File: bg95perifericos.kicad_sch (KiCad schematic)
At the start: 36 parts, among them Q10 BC817, Q11 BC817, Q2 BC817, Q3 BC817, Q4 BC817, Q5 BC817, Q6 BC817, Q7 BC817, Q8 BC817, Q9 BC817

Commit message: Inserido as informações dos sheets do modulo IoT
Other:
- company: (none) -> Magalhaes
- title: (none) -> BG95-Peripherals
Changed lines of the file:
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@@
 (kicad_sch (version 20211123) (generator eeschema)
   (paper "A4")
+  (title_block
+    (title "BG95-Peripherals")
+    (date "2022-08-10")
+    (rev "0.0.0")
+    (company "Magalhaes")
+    (comment 1 "Author: Alexandre Magalhães")
+    (comment 2 "Variant 1: Full")
+  )
   (junction (at 123.19 129.54) (diameter 0) (color 0 0 0 0)
   )
@@
       (effects (font (size 1.27 1.27)) hide)
     )
-    (property "Value" "" (id 1) (at 129.54 43.18 0))
+    (property "Value" "+3.3V" (id 1) (at 129.54 43.18 0))
     (property "Footprint" "" (id 2) (at 129.54 46.99 0)
       (effects (font (size 1.27 1.27)) hide)
@@
       (effects (font (size 1.27 1.27)) hide)
     )
-    (property "Value" "" (id 1) (at 214.63 116.84 0))
+    (property "Value" "+3.3V" (id 1) (at 214.63 116.84 0))
     (property "Footprint" "" (id 2) (at 214.63 120.65 0)
       (effects (font (size 1.27 1.27)) hide)
@@
       (effects (font (size 1.27 1.27)) hide)
     )
-    (property "Value" "" (id 1) (at 156.21 180.34 0))
+    (property "Value" "VDD_EXT" (id 1) (at 156.21 180.34 0))
     (property "Footprint" "" (id 2) (at 156.21 184.15 0)
       (effects (font (size 1.27 1.27)) hide)
@@
       (effects (font (size 1.27 1.27)) hide)
     )
-    (property "Value" "" (id 1) (at 266.7 118.11 0))
+    (property "Value" "+3.3V" (id 1) (at 266.7 118.11 0))
     (property "Footprint" "" (id 2) (at 266.7 121.92 0)
       (effects (font (size 1.27 1.27)) hide)
@@
       (effects (font (size 1.27 1.27)) hide)
     )
-    (property "Value" "" (id 1) (at 123.19 165.1 0))
+    (property "Value" "+3.3V" (id 1) (at 123.19 165.1 0))
     (property "Footprint" "" (id 2) (at 123.19 161.29 0)
       (effects (font (size 1.27 1.27)) hide)
@@
       (effects (font (size 1.27 1.27)) hide)
     )
-    (property "Value" "" (id 1) (at 54.61 165.1 0))
+    (property "Value" "+3.3V" (id 1) (at 54.61 165.1 0))
     (property "Footprint" "" (id 2) (at 54.61 161.29 0)
       (effects (font (size 1.27 1.27)) hide)
@@
       (effects (font (size 1.27 1.27)) hide)
     )
-    (property "Value" "" (id 1) (at 116.84 43.18 0))
+    (property "Value" "+3.3V" (id 1) (at 116.84 43.18 0))
     (property "Footprint" "" (id 2) (at 116.84 46.99 0)
       (effects (font (size 1.27 1.27)) hide)
@@
       (effects (font (size 1.27 1.27)) hide)
     )
-    (property "Value" "" (id 1) (at 163.83 180.34 0))
+    (property "Value" "+3.3V" (id 1) (at 163.83 180.34 0))
     (property "Footprint" "" (id 2) (at 163.83 184.15 0)
       (effects (font (size 1.27 1.27)) hide)

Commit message: Referencia dos componentes
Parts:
- renumbered R63 to R65, R64 to R66, R65 to R67, R66 to R68, R67 to R69, R68 to R70, R69 to R71, R70 to R72, R71 to R73, R72 to R74, R73 to R75, R74 to R76, R75 to R77, R76 to R78, R77 to R79, R78 to R80, R79 to R81, R80 to R82, R81 to R83, R82 to R84, R83 to R85, R84 to R86, R85 to R87, R86 to R88

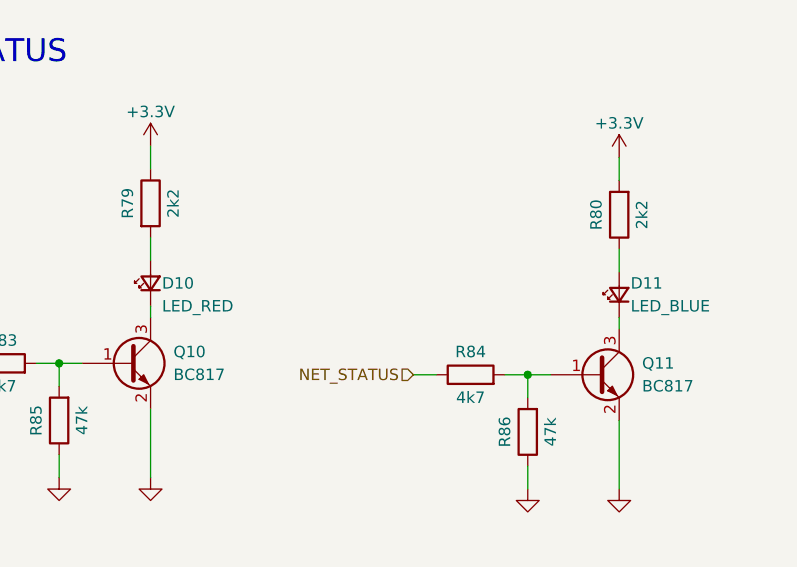
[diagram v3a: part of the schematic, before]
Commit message: Adicionado os pads dos Test Point e alterado o Bead
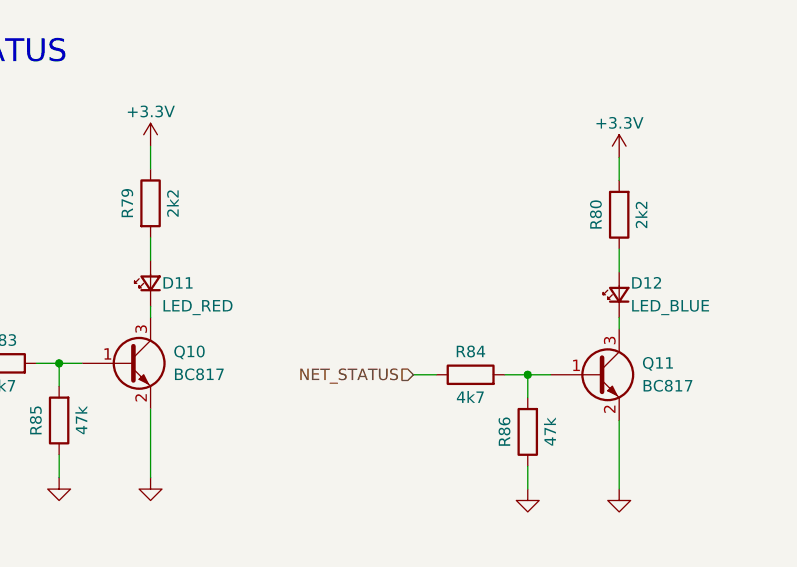
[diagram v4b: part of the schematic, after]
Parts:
- renumbered D10 to D11, D11 to D12
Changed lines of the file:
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@@
   (symbol (lib_id "power:GND") (at 35.56 87.63 0) (unit 1)
     (in_bom yes) (on_board yes) (fields_autoplaced)
-    (property "Reference" "#PWR0113" (id 0) (at 35.56 93.98 0)
+    (property "Reference" "#PWR0115" (id 0) (at 35.56 93.98 0)
       (effects (font (size 1.27 1.27)) hide)
     )
@@
   (symbol (lib_id "power:GND") (at 214.63 157.48 0) (unit 1)
     (in_bom yes) (on_board yes) (fields_autoplaced)
-    (property "Reference" "#PWR0128" (id 0) (at 214.63 163.83 0)
+    (property "Reference" "#PWR0130" (id 0) (at 214.63 163.83 0)
       (effects (font (size 1.27 1.27)) hide)
     )
@@
   (symbol (lib_id "Alexandre_Library:Power") (at 129.54 46.99 0) (unit 1)
     (in_bom yes) (on_board yes)
-    (property "Reference" "#PWR110" (id 0) (at 129.54 39.37 0)
+    (property "Reference" "#PWR112" (id 0) (at 129.54 39.37 0)
       (effects (font (size 1.27 1.27)) hide)
     )
@@
   (symbol (lib_id "Alexandre_Library:Power") (at 214.63 120.65 0) (unit 1)
     (in_bom yes) (on_board yes)
-    (property "Reference" "#PWR123" (id 0) (at 214.63 113.03 0)
+    (property "Reference" "#PWR125" (id 0) (at 214.63 113.03 0)
       (effects (font (size 1.27 1.27)) hide)
     )
@@
   (symbol (lib_id "Alexandre_Library:Power") (at 156.21 184.15 0) (unit 1)
     (in_bom yes) (on_board yes)
-    (property "Reference" "#PWR133" (id 0) (at 156.21 176.53 0)
+    (property "Reference" "#PWR135" (id 0) (at 156.21 176.53 0)
       (effects (font (size 1.27 1.27)) hide)
     )
@@
   (symbol (lib_id "Alexandre_Library:Power") (at 266.7 121.92 0) (unit 1)
     (in_bom yes) (on_board yes)
-    (property "Reference" "#PWR124" (id 0) (at 266.7 114.3 0)
+    (property "Reference" "#PWR126" (id 0) (at 266.7 114.3 0)
       (effects (font (size 1.27 1.27)) hide)
     )
@@
   (symbol (lib_id "power:GND") (at 238.76 53.34 0) (unit 1)
     (in_bom yes) (on_board yes) (fields_autoplaced)
-    (property "Reference" "#PWR0112" (id 0) (at 238.76 59.69 0)
+    (property "Reference" "#PWR0114" (id 0) (at 238.76 59.69 0)
       (effects (font (size 1.27 1.27)) hide)
     )
@@
   (symbol (lib_id "power:GND") (at 228.6 90.17 0) (unit 1)
     (in_bom yes) (on_board yes) (fields_autoplaced)
-    (property "Reference" "#PWR0119" (id 0) (at 228.6 96.52 0)
+    (property "Reference" "#PWR0121" (id 0) (at 228.6 96.52 0)
       (effects (font (size 1.27 1.27)) hide)
     )
@@
   (symbol (lib_id "power:GND") (at 256.54 158.75 0) (unit 1)
     (in_bom yes) (on_board yes) (fields_autoplaced)
-    (property "Reference" "#PWR0129" (id 0) (at 256.54 165.1 0)
+    (property "Reference" "#PWR0131" (id 0) (at 256.54 165.1 0)
       (effects (font (size 1.27 1.27)) hide)
     )
@@
   (symbol (lib_id "power:GND") (at 204.47 157.48 0) (unit 1)
     (in_bom yes) (on_board yes) (fields_autoplaced)
-    (property "Reference" "#PWR0127" (id 0) (at 204.47 163.83 0)
+    (property "Reference" "#PWR0129" (id 0) (at 204.47 163.83 0)
       (effects (font (size 1.27 1.27)) hide)
     )
@@
   (symbol (lib_id "power:GND") (at 116.84 87.63 0) (unit 1)
     (in_bom yes) (on_board yes) (fields_autoplaced)
-    (property "Reference" "#PWR0116" (id 0) (at 116.84 93.98 0)
+    (property "Reference" "#PWR0118" (id 0) (at 116.84 93.98 0)
       (effects (font (size 1.27 1.27)) hide)
     )
@@
   (symbol (lib_id "Alexandre_Library:Power") (at 101.6 137.16 0) (unit 1)
     (in_bom yes) (on_board yes)
-    (property "Reference" "#PWR126" (id 0) (at 101.6 129.54 0)
+    (property "Reference" "#PWR128" (id 0) (at 101.6 129.54 0)
       (effects (font (size 1.27 1.27)) hide)
     )
@@
   (symbol (lib_id "Device:LED_Small") (at 266.7 137.16 90) (unit 1)
     (in_bom yes) (on_board yes)
-    (property "Reference" "D11" (id 0) (at 267.97 135.89 90)
+    (property "Reference" "D12" (id 0) (at 267.97 135.89 90)
       (effects (font (size 1.27 1.27)) (justify right))
     )
@@
   (symbol (lib_id "power:GND") (at 228.6 53.34 0) (unit 1)
     (in_bom yes) (on_board yes) (fields_autoplaced)
-    (property "Reference" "#PWR0111" (id 0) (at 228.6 59.69 0)
+    (property "Reference" "#PWR0113" (id 0) (at 228.6 59.69 0)
       (effects (font (size 1.27 1.27)) hide)
     )
@@
   (symbol (lib_id "Device:LED_Small") (at 214.63 135.89 90) (unit 1)
     (in_bom yes) (on_board yes)
-    (property "Reference" "D10" (id 0) (at 215.9 135.89 90)
+    (property "Reference" "D11" (id 0) (at 215.9 135.89 90)
       (effects (font (size 1.27 1.27)) (justify right))
     )
@@
   (symbol (lib_id "Alexandre_Library:Power") (at 54.61 115.57 0) (unit 1)
     (in_bom yes) (on_board yes)
-    (property "Reference" "#PWR121" (id 0) (at 54.61 107.95 0)
+    (property "Reference" "#PWR123" (id 0) (at 54.61 107.95 0)
       (effects (font (size 1.27 1.27)) hide)
     )
@@
   (symbol (lib_id "power:GND") (at 238.76 90.17 0) (unit 1)
     (in_bom yes) (on_board yes) (fields_autoplaced)
-    (property "Reference" "#PWR0120" (id 0) (at 238.76 96.52 0)
+    (property "Reference" "#PWR0122" (id 0) (at 238.76 96.52 0)
       (effects (font (size 1.27 1.27)) hide)
     )
@@
   (symbol (lib_id "Alexandre_Library:Power") (at 123.19 161.29 180) (unit 1)
     (in_bom yes) (on_board yes)
-    (property "Reference" "#PWR132" (id 0) (at 123.19 168.91 0)
+    (property "Reference" "#PWR134" (id 0) (at 123.19 168.91 0)
       (effects (font (size 1.27 1.27)) hide)
     )
@@
   (symbol (lib_id "Alexandre_Library:Power") (at 54.61 161.29 180) (unit 1)
     (in_bom yes) (on_board yes)
-    (property "Reference" "#PWR131" (id 0) (at 54.61 168.91 0)
+    (property "Reference" "#PWR133" (id 0) (at 54.61 168.91 0)
       (effects (font (size 1.27 1.27)) hide)
     )
@@
   (symbol (lib_id "power:GND") (at 139.7 87.63 0) (unit 1)
     (in_bom yes) (on_board yes) (fields_autoplaced)
-    (property "Reference" "#PWR0118" (id 0) (at 139.7 93.98 0)
+    (property "Reference" "#PWR0120" (id 0) (at 139.7 93.98 0)
       (effects (font (size 1.27 1.27)) hide)
     )
@@
   (symbol (lib_id "power:GND") (at 266.7 158.75 0) (unit 1)
     (in_bom yes) (on_board yes) (fields_autoplaced)
-    (property "Reference" "#PWR0130" (id 0) (at 266.7 165.1 0)
+    (property "Reference" "#PWR0132" (id 0) (at 266.7 165.1 0)
       (effects (font (size 1.27 1.27)) hide)
     )
@@
   (symbol (lib_id "Alexandre_Library:Power") (at 116.84 46.99 0) (unit 1)
     (in_bom yes) (on_board yes)
-    (property "Reference" "#PWR109" (id 0) (at 116.84 39.37 0)
+    (property "Reference" "#PWR111" (id 0) (at 116.84 39.37 0)
       (effects (font (size 1.27 1.27)) hide)
     )
@@
   (symbol (lib_id "Alexandre_Library:Power") (at 35.56 46.99 0) (unit 1)
     (in_bom yes) (on_board yes)
-    (property "Reference" "#PWR107" (id 0) (at 35.56 39.37 0)
+    (property "Reference" "#PWR109" (id 0) (at 35.56 39.37 0)
       (effects (font (size 1.27 1.27)) hide)
     )
@@
   (symbol (lib_id "Alexandre_Library:Power") (at 163.83 184.15 0) (unit 1)
     (in_bom yes) (on_board yes)
-    (property "Reference" "#PWR134" (id 0) (at 163.83 176.53 0)
+    (property "Reference" "#PWR136" (id 0) (at 163.83 176.53 0)
       (effects (font (size 1.27 1.27)) hide)
     )
@@
   (symbol (lib_id "Alexandre_Library:Power") (at 48.26 46.99 0) (unit 1)
     (in_bom yes) (on_board yes)
-    (property "Reference" "#PWR108" (id 0) (at 48.26 39.37 0)
+    (property "Reference" "#PWR110" (id 0) (at 48.26 39.37 0)
       (effects (font (size 1.27 1.27)) hide)
     )
@@
   (symbol (lib_id "power:GND") (at 129.54 87.63 0) (unit 1)
     (in_bom yes) (on_board yes) (fields_autoplaced)
-    (property "Reference" "#PWR0117" (id 0) (at 129.54 93.98 0)
+    (property "Reference" "#PWR0119" (id 0) (at 129.54 93.98 0)
       (effects (font (size 1.27 1.27)) hide)
     )
@@
   (symbol (lib_id "Alexandre_Library:Power") (at 123.19 115.57 0) (unit 1)
     (in_bom yes) (on_board yes)
-    (property "Reference" "#PWR122" (id 0) (at 123.19 107.95 0)
+    (property "Reference" "#PWR124" (id 0) (at 123.19 107.95 0)
       (effects (font (size 1.27 1.27)) hide)
     )
@@
   (symbol (lib_id "power:GND") (at 58.42 87.63 0) (unit 1)
     (in_bom yes) (on_board yes) (fields_autoplaced)
-    (property "Reference" "#PWR0115" (id 0) (at 58.42 93.98 0)
+    (property "Reference" "#PWR0117" (id 0) (at 58.42 93.98 0)
       (effects (font (size 1.27 1.27)) hide)
     )
@@
   (symbol (lib_id "power:GND") (at 156.21 191.77 0) (unit 1)
     (in_bom yes) (on_board yes) (fields_autoplaced)
-    (property "Reference" "#PWR0135" (id 0) (at 156.21 198.12 0)
+    (property "Reference" "#PWR0137" (id 0) (at 156.21 198.12 0)
       (effects (font (size 1.27 1.27)) hide)
     )
@@
   (symbol (lib_id "Alexandre_Library:Power") (at 33.02 137.16 0) (unit 1)
     (in_bom yes) (on_board yes)
-    (property "Reference" "#PWR125" (id 0) (at 33.02 129.54 0)
+    (property "Reference" "#PWR127" (id 0) (at 33.02 129.54 0)
       (effects (font (size 1.27 1.27)) hide)
     )
@@
   (symbol (lib_id "power:GND") (at 48.26 87.63 0) (unit 1)
     (in_bom yes) (on_board yes) (fields_autoplaced)
-    (property "Reference" "#PWR0114" (id 0) (at 48.26 93.98 0)
-      (effects (font (size 1.27 1.27)) hide)
-    )
+    (property "Reference" "#PWR0116" (id 0) (at 48.26 93.98 0)
+      (effects (font (size 1.27 1.27)) hide)
+    )
